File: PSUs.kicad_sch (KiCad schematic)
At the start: 28 parts, among them J6 Conn_01x02, U12 CH224K, U7 AP62300WU-7, U8 AP62300WU-7

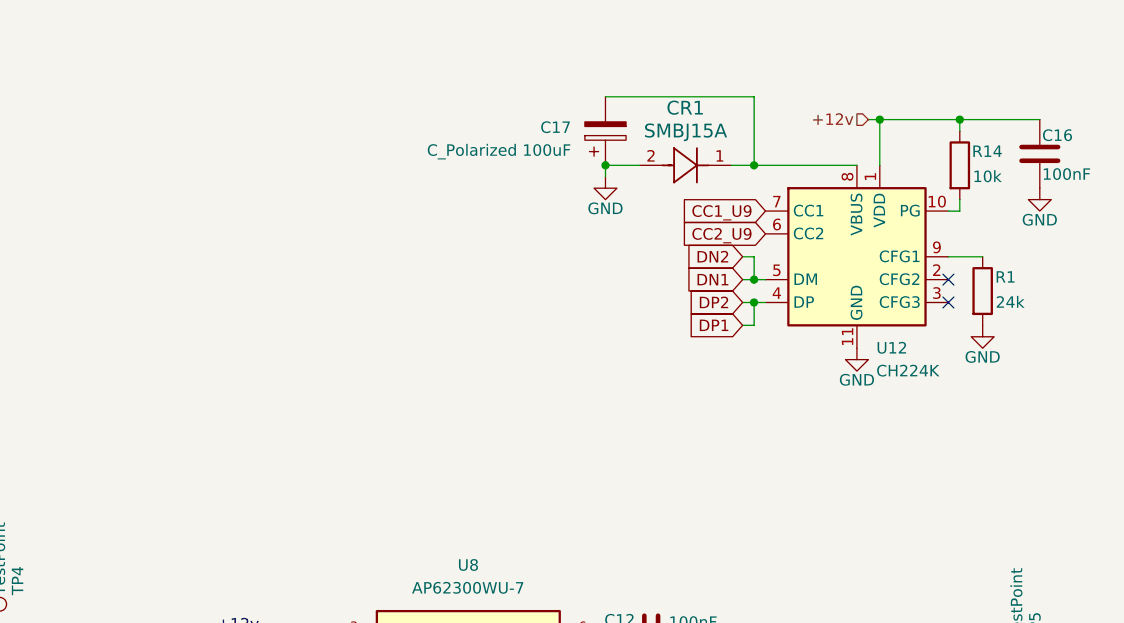
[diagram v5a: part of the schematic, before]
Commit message: Changed PD back to HUSB238
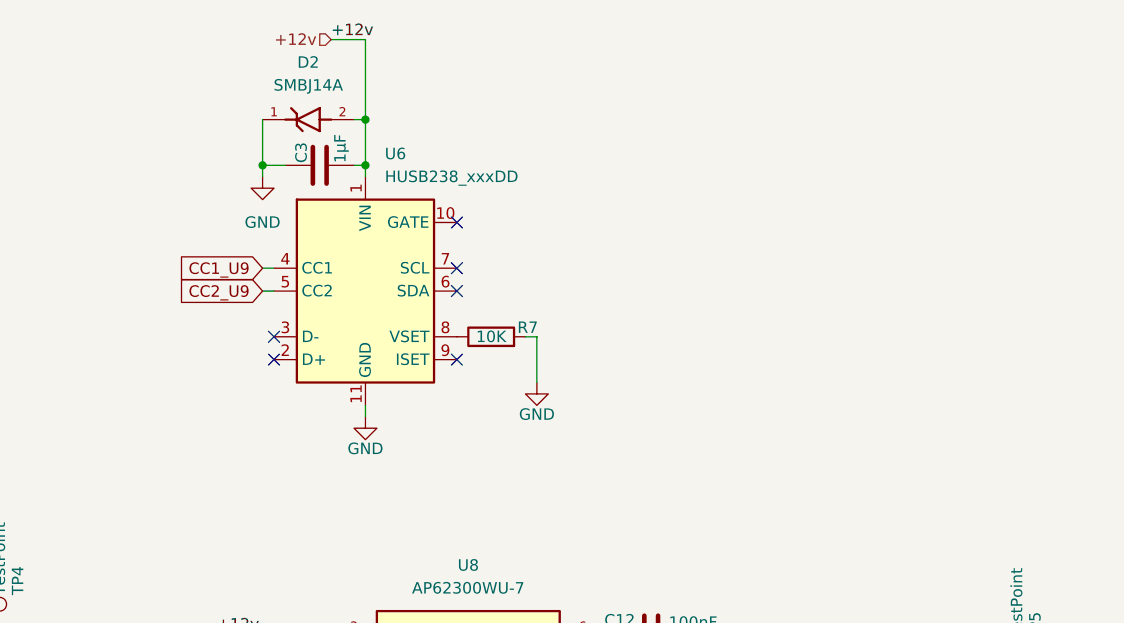
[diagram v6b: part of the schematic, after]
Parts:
- removed C16: 100nF, Capacitor_SMD:C_0402_1005Metric_Pad0.74x0.62mm_HandSolder, symbol Device:C
- removed C17: C_Polarized 100uF, Capacitor_SMD:CP_Elec_4x3, symbol Device:C_Polarized
- removed CR1: SMBJ15A, DIODE_DO214AA, symbol SMBJ15A:SMBJ15A
- removed R1: 24k, Resistor_SMD:R_0402_1005Metric_Pad0.72x0.64mm_HandSolder, symbol Device:R
- removed R14: 10k, Resistor_SMD:R_0402_1005Metric_Pad0.72x0.64mm_HandSolder, symbol Device:R
- removed U12: CH224K, Package_SO:SSOP-10-1EP_3.9x4.9mm_P1mm_EP2.1x3.3mm, symbol Interface_USB:CH224K
- added C3: 1µF, Capacitor_SMD:C_0402_1005Metric_Pad0.74x0.62mm_HandSolder, symbol Device:C
- added D2: SMBJ14A, SMBJ14A:DIOM5436X261N, symbol SMBJ14A:SMBJ14A
- added R7: 10K, Resistor_SMD:R_0402_1005Metric_Pad0.72x0.64mm_HandSolder, symbol Device:R
- added U6: HUSB238_xxxDD, Package_DFN_QFN:WDFN-10-1EP_3x3mm_P0.5mm_EP1.8x2.5mm, symbol Interface_USB:HUSB238_xxxDD
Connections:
- net CC1_U9: now also U6.4 (CC1)
- net CC2_U9: now also U6.5 (CC2)
- net DN1: no longer U11.B7 (DN2)
- net DP1: no longer U11.B6 (DP2)
- net GND: now also C3.1, D2.1, R7.2, U6.11 (GND)
- net VBUS-PD: now also C3.2, D2.2, U6.1 (VIN)
- new net: R7.1, U6.8 (VSET)
- new net DN2: U11.B7 (DN2)
- new net DP2: U11.B6 (DP2)
- no-connect marks 6 -> 10

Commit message: Adjusted footprint Phoenix connector and added some text.
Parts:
- J6: footprint TerminalBlock_Phoenix:TerminalBlock_Phoenix_MKDS-1,5-2-5.08_1x02_P5.08mm_Horizontal -> 1-2199119-5_Finley:TerminalBlock_PhoenixTerminalBlock_Phoenix_MKDS-1,5-2-5.08_1x02_P5.08mm_Horizontal_Edited
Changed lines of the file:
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@@
 			)
 		)
-		(property "Footprint" "TerminalBlock_Phoenix:TerminalBlock_Phoenix_MKDS-1,5-2-5.08_1x02_P5.08mm_Horizontal"
+		(property "Footprint" "1-2199119-5_Finley:TerminalBlock_PhoenixTerminalBlock_Phoenix_MKDS-1,5-2-5.08_1x02_P5.08mm_Horizontal_Edited"
 			(at 25.4 31.75 0)
 			(effects

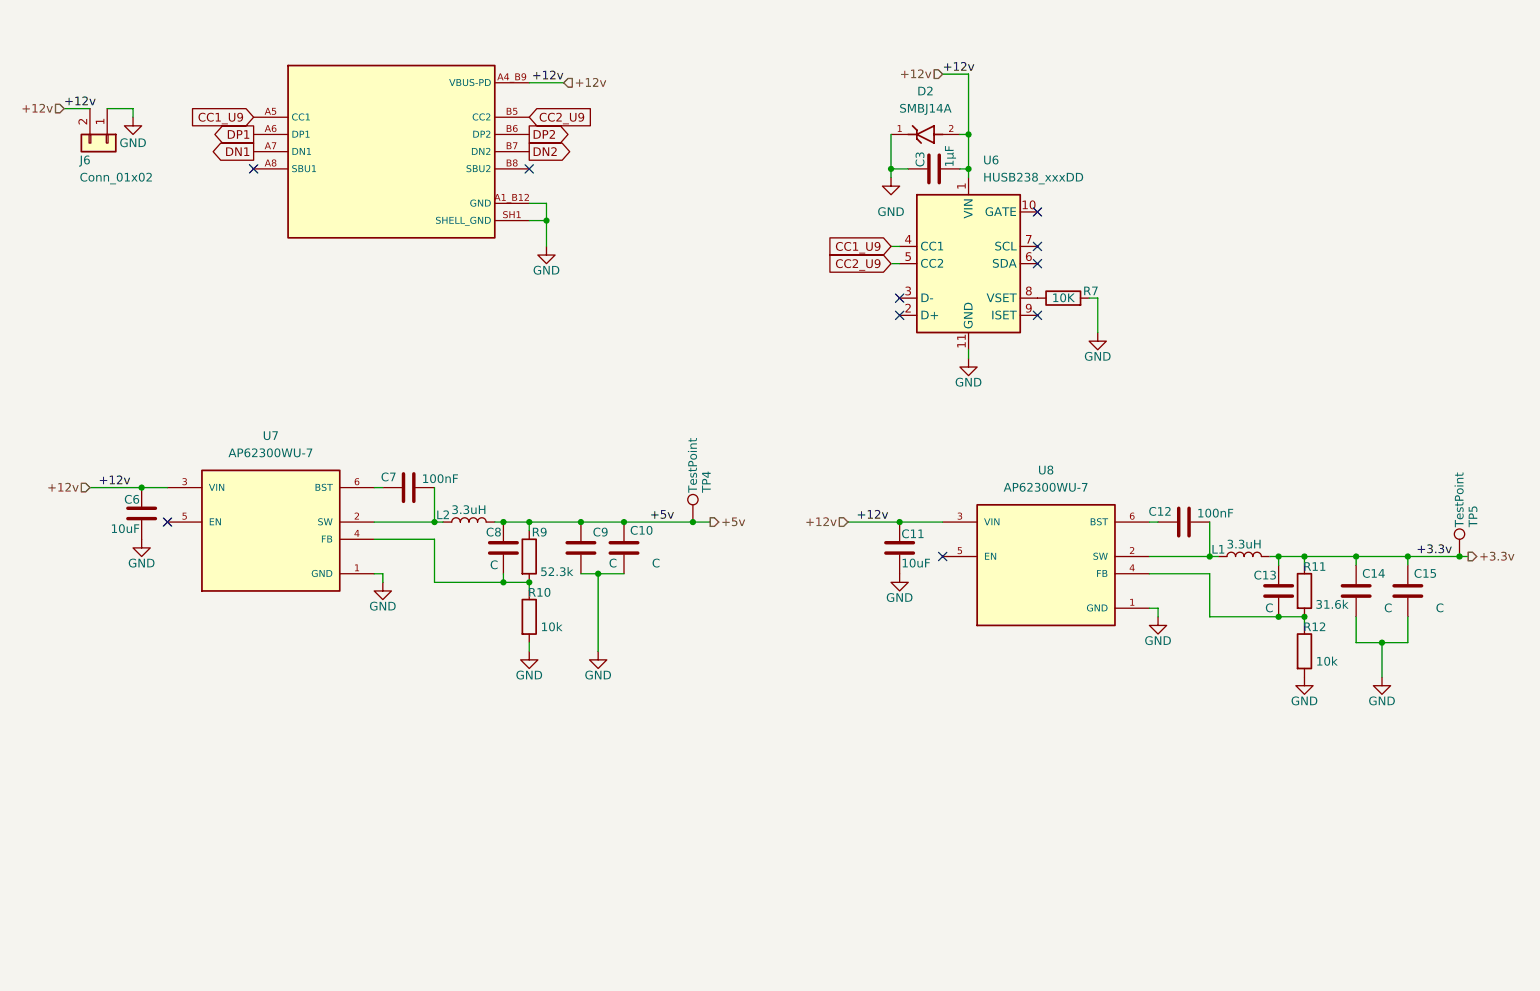
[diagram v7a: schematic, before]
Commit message: Added datasheets for to-be-ordered components, double checked BOM
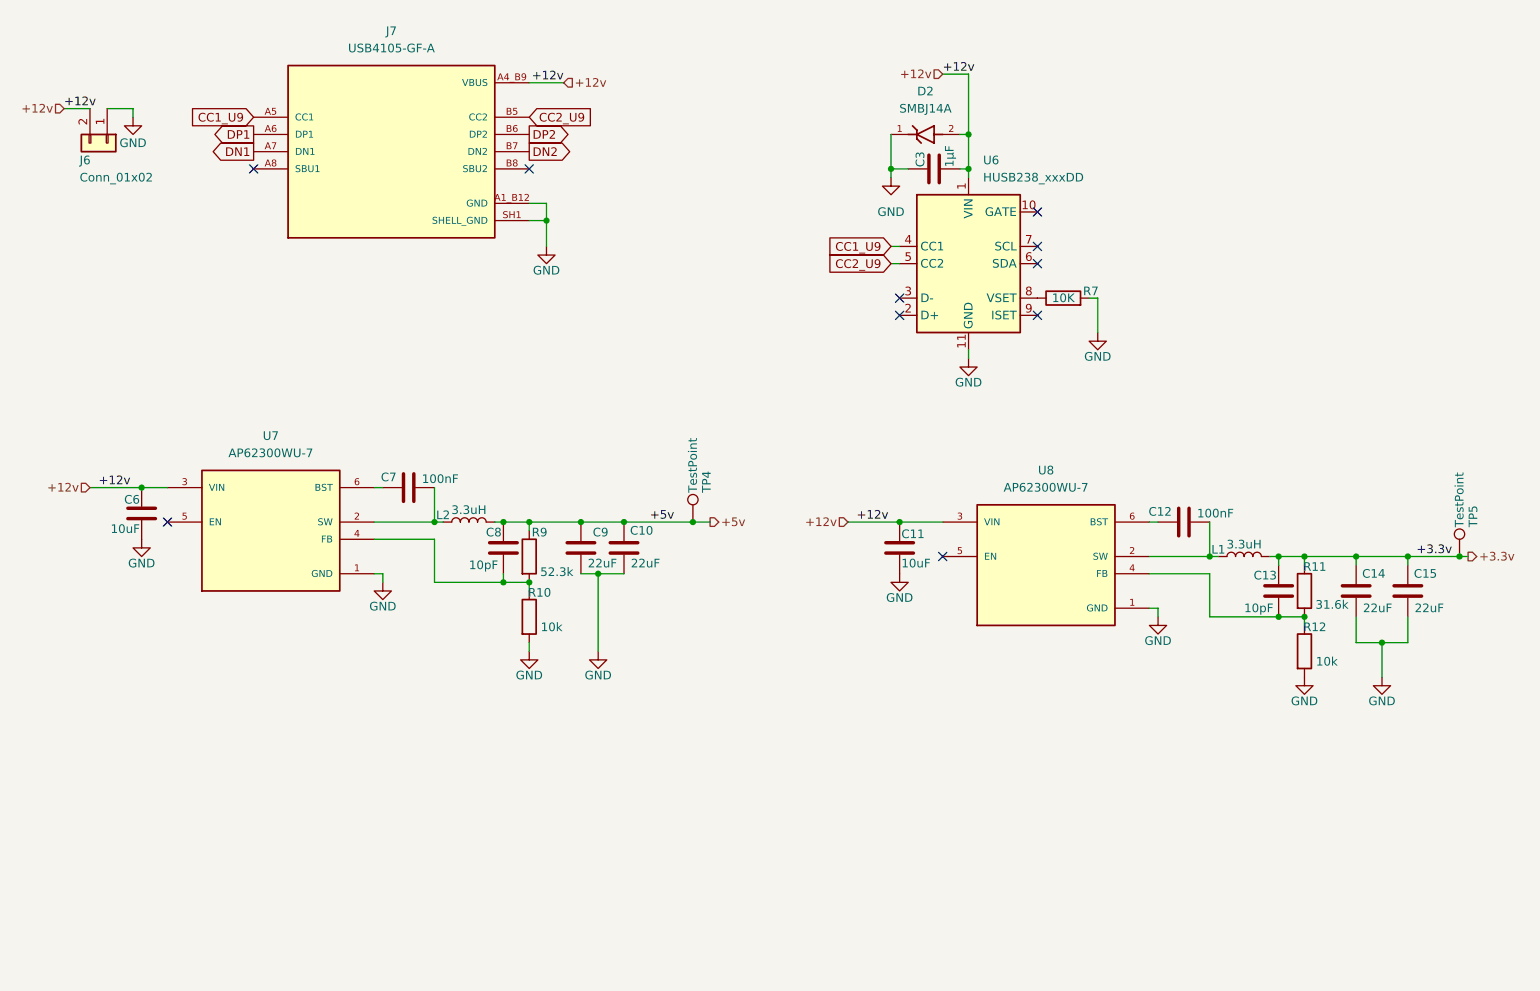
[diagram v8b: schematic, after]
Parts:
- removed U11: ~, symbol USB4105-GF-A:USB4105-GF-A-PD
- added J7: USB4105-GF-A, USB4105-GF-A:GCT_USB4105-GF-A, symbol USB4105-GF-A:USB4105-GF-A
- C10, C14, C15, C9: value C -> 22uF
- C13, C8: value C -> 10pF
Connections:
- net CC1_U9: now also J7.A5 (CC1)
- net CC2_U9: now also J7.B5 (CC2)
- net DN1: now also J7.A7 (DN1)
- net DN2: now also J7.B7 (DN2)
- net DP1: now also J7.A6 (DP1)
- net DP2: now also J7.B6 (DP2)
- net GND: now also J7.A1_B12 (GND), J7.B1_A12 (GND), J7.SH1 (SHELL_GND), J7.SH2 (SHELL_GND), J7.SH3 (SHELL_GND), J7.SH4 (SHELL_GND)
- net VBUS-PD renamed VBUS
- net VBUS: now also J7.A4_B9 (VBUS), J7.B4_A9 (VBUS)
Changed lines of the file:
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@@
-	)
-	(symbol
-		(lib_id "USB4105-GF-A:USB4105-GF-A-PD")
-		(at 66.04 33.02 0)
-		(unit 1)
-		(exclude_from_sim no)
-		(in_bom yes)
-		(on_board yes)
-		(dnp no)
-		(fields_autoplaced yes)
-		(property "Reference" "U11"
-			(at 66.04 33.02 0)
-			(effects
-				(font
-					(size 1.27 1.27)
-				)
-				(hide yes)
-			)
-		)
-		(property "Value" "~"
-			(at 67.31 17.78 0)
-			(effects
-				(font
-					(size 1.27 1.27)
-				)
-			)
-		)
-		(property "Footprint" ""
-			(at 66.04 33.02 0)
-			(effects
-				(font
-					(size 1.27 1.27)
-				)
-				(hide yes)
-			)
-		)
-		(property "Datasheet" ""
-			(at 66.04 33.02 0)
-			(effects
-				(font
-					(size 1.27 1.27)
-				)
-				(hide yes)
-			)
-		)
-		(property "Description" ""
-			(at 66.04 33.02 0)
-			(effects
-				(font
-					(size 1.27 1.27)
-				)
-				(hide yes)
-			)
-		)
-		(pin "A5"
-		)
-		(pin "A7"
-		)
-		(pin "A8"
-		)
-		(pin "B5"
-		)
-		(pin "A6"
-		)
-		(pin "B7"
-		)
-		(pin "B6"
-		)
-		(pin "A1_B12"
-		)
-		(pin "SH1"
-		)
-		(pin "SH3"
-		)
-		(pin "B8"
-		)
-		(pin "B1_A12"
-		)
-		(pin "SH2"
-		)
-		(pin "SH4"
-		)
-		(pin "B4_A9"
-		)
-		(pin "A4_B9"
-		)
-		(instances
-			(project ""
-				(path "/27bae9d5-8d47-4d02-9c9d-2650041a529b/1710a55d-c4fa-4b6a-99e2-6054aab87aa6"
-					(reference "U11")
-					(unit 1)
-				)
-			)
-		)
 	)
 	(symbol
@@
 			)
 		)
-		(property "Value" "C"
+		(property "Value" "10pF"
 			(at 83.058 93.98 0)
 			(effects
@@
 	)
 	(symbol
+		(lib_id "USB4105-GF-A:USB4105-GF-A")
+		(at 67.31 33.02 0)
+		(unit 1)
+		(exclude_from_sim no)
+		(in_bom yes)
+		(on_board yes)
+		(dnp no)
+		(fields_autoplaced yes)
+		(property "Reference" "J7"
+			(at 67.31 15.24 0)
+			(effects
+				(font
+					(size 1.27 1.27)
+				)
+			)
+		)
+		(property "Value" "USB4105-GF-A"
+			(at 67.31 17.78 0)
+			(effects
+				(font
+					(size 1.27 1.27)
+				)
+			)
+		)
+		(property "Footprint" "USB4105-GF-A:GCT_USB4105-GF-A"
+			(at 67.31 33.02 0)
+			(effects
+				(font
+					(size 1.27 1.27)
+				)
+				(justify bottom)
+				(hide yes)
+			)
+		)
+		(property "Datasheet" ""
+			(at 67.31 33.02 0)
+			(effects
+				(font
+					(size 1.27 1.27)
+				)
+				(hide yes)
+			)
+		)
+		(property "Description" ""
+			(at 67.31 33.02 0)
+			(effects
+				(font
+					(size 1.27 1.27)
+				)
+				(hide yes)
+			)
+		)
+		(property "MF" "GCT"
+			(at 67.31 33.02 0)
+			(effects
+				(font
+					(size 1.27 1.27)
+				)
+				(justify bottom)
+				(hide yes)
+			)
+		)
+		(property "MAXIMUM_PACKAGE_HEIGHT" "3.31 mm"
+			(at 67.31 33.02 0)
+			(effects
+				(font
+					(size 1.27 1.27)
+				)
+				(justify bottom)
+				(hide yes)
+			)
+		)
+		(property "Package" "None"
+			(at 67.31 33.02 0)
+			(effects
+				(font
+					(size 1.27 1.27)
+				)
+				(justify bottom)
+				(hide yes)
+			)
+		)
+		(property "Price" "None"
+			(at 67.31 33.02 0)
+			(effects
+				(font
+					(size 1.27 1.27)
+				)
+				(justify bottom)
+				(hide yes)
+			)
+		)
+		(property "Check_prices" "https://www.snapeda.com/parts/USB4105-GF-A/Global+Connector+Technology/view-part/?ref=eda"
+			(at 67.31 33.02 0)
+			(effects
+				(font
+					(size 1.27 1.27)
+				)
+				(justify bottom)
+				(hide yes)
+			)
+		)
+		(property "STANDARD" "Manufacturer Recommendations"
+			(at 67.31 33.02 0)
+			(effects
+				(font
+					(size 1.27 1.27)
+				)
+				(justify bottom)
+				(hide yes)
+			)
+		)
+		(property "PARTREV" "B4"
+			(at 67.31 33.02 0)
+			(effects
+				(font
+					(size 1.27 1.27)
+				)
+				(justify bottom)
+				(hide yes)
+			)
+		)
+		(property "SnapEDA_Link" "https://www.snapeda.com/parts/USB4105-GF-A/Global+Connector+Technology/view-part/?ref=snap"
+			(at 67.31 33.02 0)
+			(effects
+				(font
+					(size 1.27 1.27)
+				)
+				(justify bottom)
+				(hide yes)
+			)
+		)
+		(property "MP" "USB4105-GF-A"
+			(at 67.31 33.02 0)
+			(effects
+				(font
+					(size 1.27 1.27)
+				)
+				(justify bottom)
+				(hide yes)
+			)
+		)
+		(property "Description_1" "USB-C (USB TYPE-C) USB 2.0 Receptacle Connector 24 (16+8 Dummy) Position Surface Mount, Right Angle; Through Hole"
+			(at 67.31 33.02 0)
+			(effects
+				(font
+					(size 1.27 1.27)
+				)
+				(justify bottom)
+				(hide yes)
+			)
+		)
+		(property "Availability" "In Stock"
+			(at 67.31 33.02 0)
+			(effects
+				(font
+					(size 1.27 1.27)
+				)
+				(justify bottom)
+				(hide yes)
+			)
+		)
+		(property "MANUFACTURER" "GCT"
+			(at 67.31 33.02 0)
+			(effects
+				(font
+					(size 1.27 1.27)
+				)
+				(justify bottom)
+				(hide yes)
+			)
+		)
+		(pin "A6"
+		)
+		(pin "A8"
+		)
+		(pin "B4_A9"
+		)
+		(pin "B7"
+		)
+		(pin "SH2"
+		)
+		(pin "A5"
+		)
+		(pin "A7"
+		)
+		(pin "A4_B9"
+		)
+		(pin "B5"
+		)
+		(pin "B6"
+		)
+		(pin "B8"
+		)
+		(pin "A1_B12"
+		)
+		(pin "B1_A12"
+		)
+		(pin "SH1"
+		)
+		(pin "SH3"
+		)
+		(pin "SH4"
+		)
+		(instances
+			(project "ANE21_PCB"
+				(path "/27bae9d5-8d47-4d02-9c9d-2650041a529b/1710a55d-c4fa-4b6a-99e2-6054aab87aa6"
+					(reference "J7")
+					(unit 1)
+				)
+			)
+		)
+	)
+	(symbol
 		(lib_id "Device:R")
 		(at 166.37 54.61 90)
@@
 			)
 		)
-		(property "Value" "C"
+		(property "Value" "22uF"
 			(at 100.584 93.726 0)
 			(effects
@@
 			)
 		)
-		(property "Value" "C"
+		(property "Value" "22uF"
 			(at 106.934 93.726 0)
 			(effects
@@
 			)
 		)
-		(property "Value" "C"
+		(property "Value" "22uF"
 			(at 214.884 100.33 0)
 			(effects
@@
 			)
 		)
-		(property "Value" "C"
+		(property "Value" "10pF"
 			(at 197.358 100.33 0)
 			(effects
@@
 			)
 		)
-		(property "Value" "C"
+		(property "Value" "22uF"
 			(at 222.504 100.33 0)
 			(effects
